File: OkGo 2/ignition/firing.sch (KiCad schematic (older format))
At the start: 75 parts, among them K201 16A SPST, K202 16A SPST, K203 16A SPST, K204 16A SPST, K205 16A SPST, P201 CH3_LED, P202 CH3_LED, P203 CH3, P204 CH1_LED, P205 CH1_LED, P206 CH1, P207 CH4_LED, P208 CH4_LED, P209 CH4, P210 CH2_LED, P211 CH2_LED, P212 CH2, Q201 BSS138BK, Q202 BSS138BK, Q203 BSS138BK, Q204 BSS138BK, Q205 BSS138BK, U201 BEZEL, U202 BEZEL, U203 BEZEL, U204 BEZEL

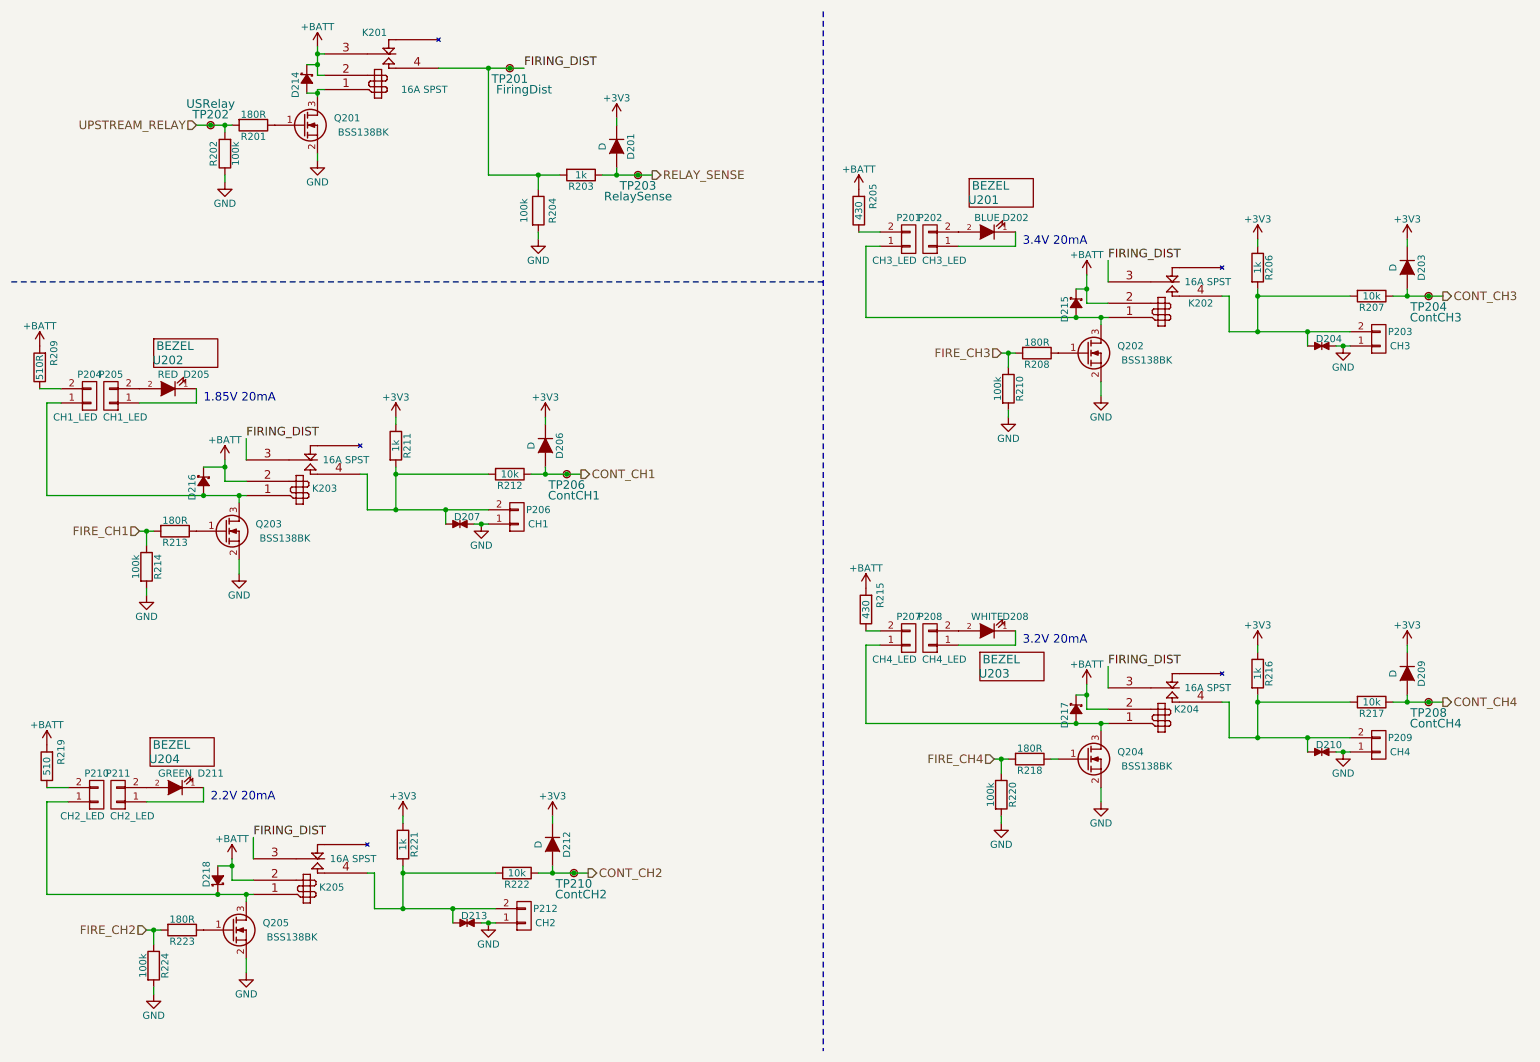
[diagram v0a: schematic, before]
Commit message: Lots more footprinting, mostly done.
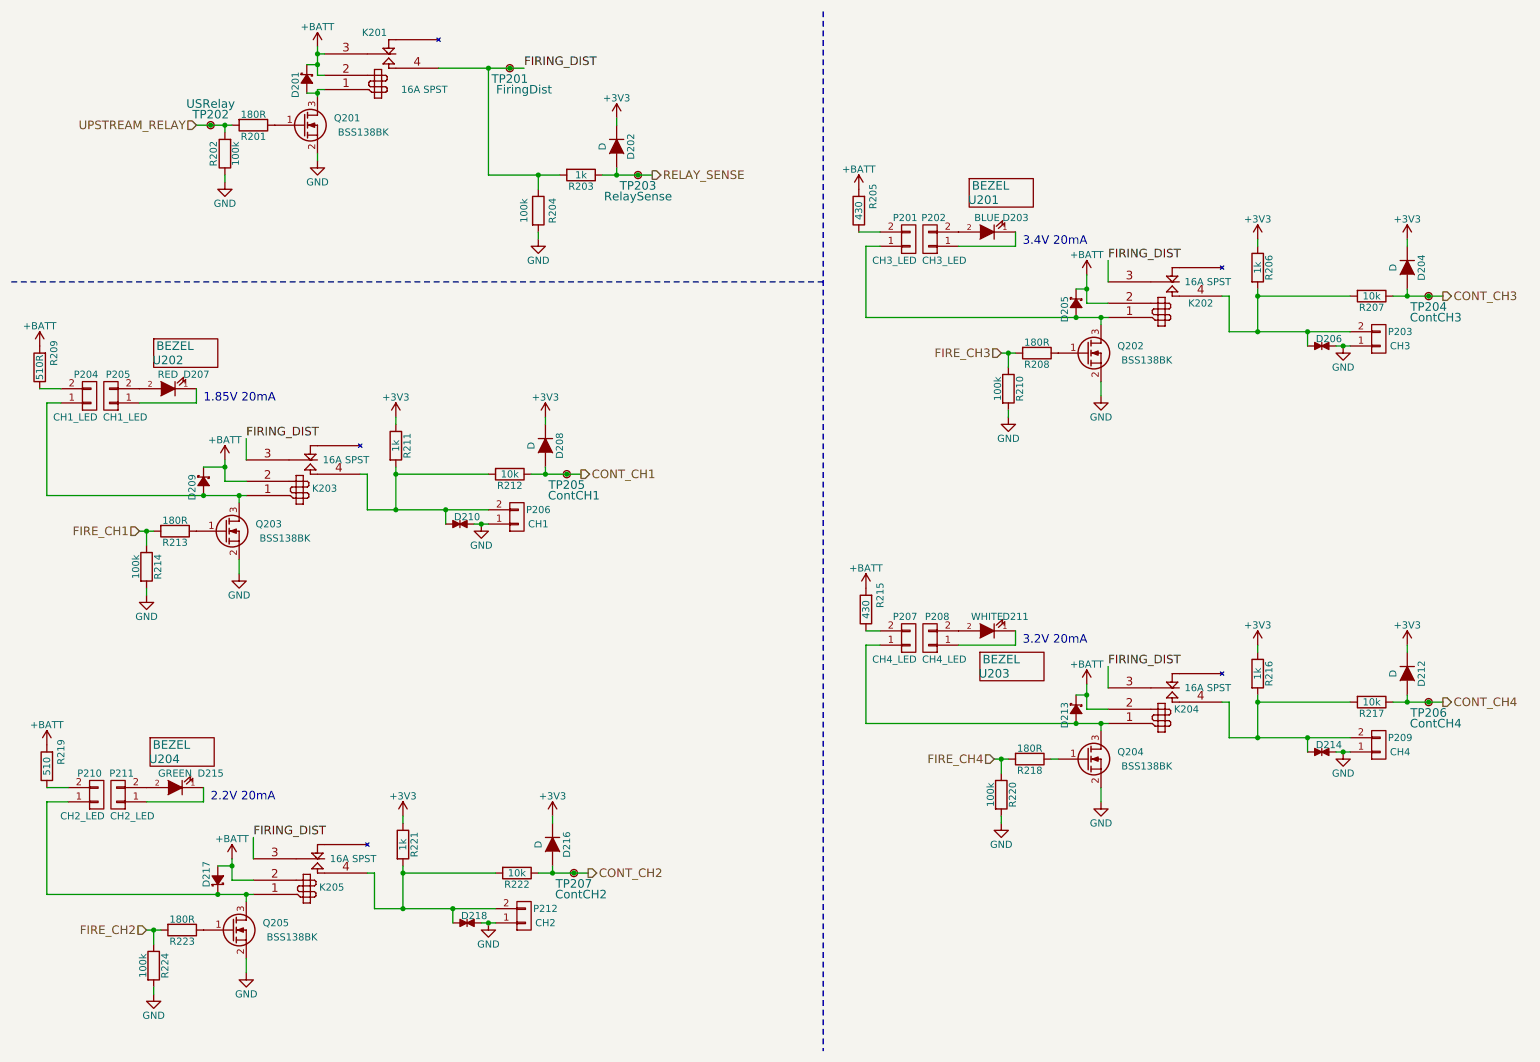
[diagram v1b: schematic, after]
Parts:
- K201, K202, K203, K204, K205: footprint (none) -> ignition:Relay_RT314
- P201, P204, P207, P210: footprint (none) -> common:JST-PA-2; Farnell (none) -> 1830747
- P202, P205, P208, P211: Farnell (none) -> 1830726
- P203, P206, P209, P212: footprint (none) -> ignition:2-wire
- Q202: footprint (none) -> Housings_SOT-23_SOT-143_TSOT-6:SOT-23
- R202, R204, R210, R214, R220, R224: Farnell 2331783 -> 2331823
- renumbered D214 to D201, D201 to D202, D202 to D203, D203 to D204, D215 to D205, D204 to D206, D205 to D207, D206 to D208, D216 to D209, D207 to D210, D208 to D211, D209 to D212, D217 to D213, D210 to D214, D211 to D215, D212 to D216, D218 to D217, D213 to D218, TP206 to TP205, TP208 to TP206, TP210 to TP207

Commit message: Non-handsoldering footprints, fixes #17
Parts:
- D206, D210, D214, D218: footprint Resistors_SMD:R_0603_HandSoldering -> Resistors_SMD:R_0603
- R201, R202, R203, R204, R205, R206, R207, R208, R209, R210, R211, R212, R213, R214, R215, R216, R217, R218, R219, R220, R221, R222, R223, R224: footprint Resistors_SMD:R_0805_HandSoldering -> Resistors_SMD:R_0805
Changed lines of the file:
@@
 F 0 "R202" V 2080 1500 50  0000 C CNN
 F 1 "100k" V 1925 1500 50  0000 C CNN
-F 2 "Resistors_SMD:R_0805_HandSoldering" V 1930 1500 30  0001 C CNN
+F 2 "Resistors_SMD:R_0805" V 1930 1500 30  0001 C CNN
 F 3 "" H 2000 1500 30  0000 C CNN
 F 4 "2331823" H 2000 1500 60  0001 C CNN "Farnell"
@@
 F 0 "R201" V 2280 1300 50  0000 C CNN
 F 1 "180R" V 2125 1300 50  0000 C CNN
-F 2 "Resistors_SMD:R_0805_HandSoldering" V 2130 1300 30  0001 C CNN
+F 2 "Resistors_SMD:R_0805" V 2130 1300 30  0001 C CNN
 F 3 "" H 2200 1300 30  0000 C CNN
 F 4 "2331786" H 2200 1300 60  0001 C CNN "Farnell"
@@
 F 0 "R204" V 4300 1900 50  0000 C CNN
 F 1 "100k" V 4100 1900 50  0000 C CNN
-F 2 "Resistors_SMD:R_0805_HandSoldering" V 4130 1900 30  0001 C CNN
+F 2 "Resistors_SMD:R_0805" V 4130 1900 30  0001 C CNN
 F 3 "" H 4200 1900 30  0000 C CNN
 F 4 "2331823" H 4200 1900 60  0001 C CNN "Farnell"
@@
 F 0 "R203" V 4580 1650 50  0000 C CNN
 F 1 "1k" V 4500 1650 50  0000 C CNN
-F 2 "Resistors_SMD:R_0805_HandSoldering" V 4430 1650 30  0001 C CNN
+F 2 "Resistors_SMD:R_0805" V 4430 1650 30  0001 C CNN
 F 3 "" H 4500 1650 30  0000 C CNN
 F 4 "2331796" H 4500 1650 60  0001 C CNN "Farnell"
@@
 F 0 "R211" V 3280 3550 50  0000 C CNN
 F 1 "1k" V 3200 3550 50  0000 C CNN
-F 2 "Resistors_SMD:R_0805_HandSoldering" V 3130 3550 30  0001 C CNN
+F 2 "Resistors_SMD:R_0805" V 3130 3550 30  0001 C CNN
 F 3 "" H 3200 3550 30  0000 C CNN
 F 4 "2331796" H 3200 3550 60  0001 C CNN "Farnell"
@@
 F 0 "R214" V 1530 4400 50  0000 C CNN
 F 1 "100k" V 1375 4400 50  0000 C CNN
-F 2 "Resistors_SMD:R_0805_HandSoldering" V 1380 4400 30  0001 C CNN
+F 2 "Resistors_SMD:R_0805" V 1380 4400 30  0001 C CNN
 F 3 "" H 1450 4400 30  0000 C CNN
 F 4 "2331823" H 1450 4400 60  0001 C CNN "Farnell"
@@
 F 0 "R212" V 4080 3750 50  0000 C CNN
 F 1 "10k" V 4000 3750 50  0000 C CNN
-F 2 "Resistors_SMD:R_0805_HandSoldering" V 3930 3750 30  0001 C CNN
+F 2 "Resistors_SMD:R_0805" V 3930 3750 30  0001 C CNN
 F 3 "" H 4000 3750 30  0000 C CNN
 F 4 "2331808" H 4000 3750 60  0001 C CNN "Farnell"
@@
 F 0 "R221" V 3330 6350 50  0000 C CNN
 F 1 "1k" V 3250 6350 50  0000 C CNN
-F 2 "Resistors_SMD:R_0805_HandSoldering" V 3180 6350 30  0001 C CNN
+F 2 "Resistors_SMD:R_0805" V 3180 6350 30  0001 C CNN
 F 3 "" H 3250 6350 30  0000 C CNN
 F 4 "2331796" H 3250 6350 60  0001 C CNN "Farnell"
@@
 F 0 "R224" V 1580 7200 50  0000 C CNN
 F 1 "100k" V 1425 7200 50  0000 C CNN
-F 2 "Resistors_SMD:R_0805_HandSoldering" V 1430 7200 30  0001 C CNN
+F 2 "Resistors_SMD:R_0805" V 1430 7200 30  0001 C CNN
 F 3 "" H 1500 7200 30  0000 C CNN
 F 4 "2331823" H 1500 7200 60  0001 C CNN "Farnell"
@@
 F 0 "R222" V 4130 6550 50  0000 C CNN
 F 1 "10k" V 4050 6550 50  0000 C CNN
-F 2 "Resistors_SMD:R_0805_HandSoldering" V 3980 6550 30  0001 C CNN
+F 2 "Resistors_SMD:R_0805" V 3980 6550 30  0001 C CNN
 F 3 "" H 4050 6550 30  0000 C CNN
 F 4 "2331808" H 4050 6550 60  0001 C CNN "Farnell"
@@
 F 0 "R206" V 9330 2300 50  0000 C CNN
 F 1 "1k" V 9250 2300 50  0000 C CNN
-F 2 "Resistors_SMD:R_0805_HandSoldering" V 9180 2300 30  0001 C CNN
+F 2 "Resistors_SMD:R_0805" V 9180 2300 30  0001 C CNN
 F 3 "" H 9250 2300 30  0000 C CNN
 F 4 "2331796" H 9250 2300 60  0001 C CNN "Farnell"
@@
 F 0 "R210" V 7580 3150 50  0000 C CNN
 F 1 "100k" V 7425 3150 50  0000 C CNN
-F 2 "Resistors_SMD:R_0805_HandSoldering" V 7430 3150 30  0001 C CNN
+F 2 "Resistors_SMD:R_0805" V 7430 3150 30  0001 C CNN
 F 3 "" H 7500 3150 30  0000 C CNN
 F 4 "2331823" H 7500 3150 60  0001 C CNN "Farnell"
@@
 F 0 "R207" V 10130 2500 50  0000 C CNN
 F 1 "10k" V 10050 2500 50  0000 C CNN
-F 2 "Resistors_SMD:R_0805_HandSoldering" V 9980 2500 30  0001 C CNN
+F 2 "Resistors_SMD:R_0805" V 9980 2500 30  0001 C CNN
 F 3 "" H 10050 2500 30  0000 C CNN
 F 4 "2331808" H 10050 2500 60  0001 C CNN "Farnell"
@@
 F 0 "R216" V 9330 5150 50  0000 C CNN
 F 1 "1k" V 9250 5150 50  0000 C CNN
-F 2 "Resistors_SMD:R_0805_HandSoldering" V 9180 5150 30  0001 C CNN
+F 2 "Resistors_SMD:R_0805" V 9180 5150 30  0001 C CNN
 F 3 "" H 9250 5150 30  0000 C CNN
 F 4 "2331796" H 9250 5150 60  0001 C CNN "Farnell"
@@
 F 0 "R220" V 7530 6000 50  0000 C CNN
 F 1 "100k" V 7375 6000 50  0000 C CNN
-F 2 "Resistors_SMD:R_0805_HandSoldering" V 7380 6000 30  0001 C CNN
+F 2 "Resistors_SMD:R_0805" V 7380 6000 30  0001 C CNN
 F 3 "" H 7450 6000 30  0000 C CNN
 F 4 "2331823" H 7450 6000 60  0001 C CNN "Farnell"
@@
 F 0 "R217" V 10130 5350 50  0000 C CNN
 F 1 "10k" V 10050 5350 50  0000 C CNN
-F 2 "Resistors_SMD:R_0805_HandSoldering" V 9980 5350 30  0001 C CNN
+F 2 "Resistors_SMD:R_0805" V 9980 5350 30  0001 C CNN
 F 3 "" H 10050 5350 30  0000 C CNN
 F 4 "2331808" H 10050 5350 60  0001 C CNN "Farnell"
@@
 F 0 "R213" V 1730 4150 50  0000 C CNN
 F 1 "180R" V 1575 4150 50  0000 C CNN
-F 2 "Resistors_SMD:R_0805_HandSoldering" V 1580 4150 30  0001 C CNN
+F 2 "Resistors_SMD:R_0805" V 1580 4150 30  0001 C CNN
 F 3 "" H 1650 4150 30  0000 C CNN
 F 4 "2331786" H 1650 4150 60  0001 C CNN "Farnell"
@@
 F 0 "R223" V 1780 6950 50  0000 C CNN
 F 1 "180R" V 1625 6950 50  0000 C CNN
-F 2 "Resistors_SMD:R_0805_HandSoldering" V 1630 6950 30  0001 C CNN
+F 2 "Resistors_SMD:R_0805" V 1630 6950 30  0001 C CNN
 F 3 "" H 1700 6950 30  0000 C CNN
 F 4 "2331786" H 1700 6950 60  0001 C CNN "Farnell"
@@
 F 0 "R208" V 7780 2900 50  0000 C CNN
 F 1 "180R" V 7625 2900 50  0000 C CNN
-F 2 "Resistors_SMD:R_0805_HandSoldering" V 7630 2900 30  0001 C CNN
+F 2 "Resistors_SMD:R_0805" V 7630 2900 30  0001 C CNN
 F 3 "" H 7700 2900 30  0000 C CNN
 F 4 "2331786" H 7700 2900 60  0001 C CNN "Farnell"
@@
 F 0 "R218" V 7730 5750 50  0000 C CNN
 F 1 "180R" V 7575 5750 50  0000 C CNN
-F 2 "Resistors_SMD:R_0805_HandSoldering" V 7580 5750 30  0001 C CNN
+F 2 "Resistors_SMD:R_0805" V 7580 5750 30  0001 C CNN
 F 3 "" H 7650 5750 30  0000 C CNN
 F 4 "2331786" H 7650 5750 60  0001 C CNN "Farnell"
@@
 F 0 "D210" H 3700 4150 50  0000 C CNN
 F 1 "TVS_small" H 3650 4025 50  0001 C CNN
-F 2 "Resistors_SMD:R_0603_HandSoldering" H 3650 4100 60  0001 C CNN
+F 2 "Resistors_SMD:R_0603" H 3650 4100 60  0001 C CNN
 F 3 "" H 3650 4100 60  0000 C CNN
 F 4 "2368174" H 3650 4100 60  0001 C CNN "Farnell"
@@
 F 0 "R209" V 600 2900 50  0000 C CNN
 F 1 "510R" V 700 3000 50  0000 C CNN
-F 2 "Resistors_SMD:R_0805_HandSoldering" V 630 3000 30  0001 C CNN
+F 2 "Resistors_SMD:R_0805" V 630 3000 30  0001 C CNN
 F 3 "" H 700 3000 30  0000 C CNN
 	1    700  3000
@@
 F 0 "D218" H 3750 6950 50  0000 C CNN
 F 1 "TVS_small" H 3700 6825 50  0001 C CNN
-F 2 "Resistors_SMD:R_0603_HandSoldering" H 3700 6900 60  0001 C CNN
+F 2 "Resistors_SMD:R_0603" H 3700 6900 60  0001 C CNN
 F 3 "" H 3700 6900 60  0000 C CNN
 F 4 "2368174" H 3700 6900 60  0001 C CNN "Farnell"
@@
 F 0 "R219" V 650 5700 50  0000 C CNN
 F 1 "510" V 750 5800 50  0000 C CNN
-F 2 "Resistors_SMD:R_0805_HandSoldering" V 680 5800 30  0001 C CNN
+F 2 "Resistors_SMD:R_0805" V 680 5800 30  0001 C CNN
 F 3 "" H 750 5800 30  0000 C CNN
 	1    750  5800
@@
 F 0 "D206" H 9750 2900 50  0000 C CNN
 F 1 "TVS_small" H 9700 2775 50  0001 C CNN
-F 2 "Resistors_SMD:R_0603_HandSoldering" H 9700 2850 60  0001 C CNN
+F 2 "Resistors_SMD:R_0603" H 9700 2850 60  0001 C CNN
 F 3 "" H 9700 2850 60  0000 C CNN
 F 4 "2368174" H 9700 2850 60  0001 C CNN "Farnell"
@@
 F 0 "R205" V 6350 1800 50  0000 C CNN
 F 1 "430" V 6450 1900 50  0000 C CNN
-F 2 "Resistors_SMD:R_0805_HandSoldering" V 6380 1900 30  0001 C CNN
+F 2 "Resistors_SMD:R_0805" V 6380 1900 30  0001 C CNN
 F 3 "" H 6450 1900 30  0000 C CNN
 	1    6450 1900
@@
 F 0 "D214" H 9750 5750 50  0000 C CNN
 F 1 "TVS_small" H 9700 5625 50  0001 C CNN
-F 2 "Resistors_SMD:R_0603_HandSoldering" H 9700 5700 60  0001 C CNN
+F 2 "Resistors_SMD:R_0603" H 9700 5700 60  0001 C CNN
 F 3 "" H 9700 5700 60  0000 C CNN
 F 4 "2368174" H 9700 5700 60  0001 C CNN "Farnell"
@@
 F 0 "R215" V 6400 4600 50  0000 C CNN
 F 1 "430" V 6500 4700 50  0000 C CNN
-F 2 "Resistors_SMD:R_0805_HandSoldering" V 6430 4700 30  0001 C CNN
+F 2 "Resistors_SMD:R_0805" V 6430 4700 30  0001 C CNN
 F 3 "" H 6500 4700 30  0000 C CNN
 	1    6500 4700

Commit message: Footprinting, rockers
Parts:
- D202, D204, D208, D212, D216: footprint Diodes_SMD:SOD-123 -> ignition:SOD-123F
- P203, P206, P209, P212: footprint ignition:2-wire -> ignition:PCB_SPADE; Farnell (none) -> 2308798
